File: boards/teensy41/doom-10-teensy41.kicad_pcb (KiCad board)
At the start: 4 copper layers, 172 x 68 mm, 73 parts, among them J1 SJ1-3525N, J2 S2B-PH-K-S(LF)(SN), J5 S2B-PH-K-S(LF)(SN), SW12 JS102011SAQN, U1 TEENSY41, U2 PCM5102APWR, U3 PAM8403DR, U4 BQ24074RGTR, U5 MAX17048G+T10, U6 TPS61023DRLR

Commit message: PCBKit's mark and pcbkit.io on every board; the RP2350 handheld ready to order
The handheld runs from two 18650 cells in parallel behind a DW01A protector and a reverse-cell
P-MOSFET, charged at up to 500 mA from the Pico's USB-C by a BQ24075 (power path into VSYS, timers
off for 6 Ah), with an on/off switch on 3V3_EN, M3 holes, ground pours and the console on pads.
Every assembled part has a JLCPCB code in stock (Basic where there is one); the module sockets are
in the BOM, the modules listed in the order's README. Check complete, the ready review clean.
Every board: routed and checked complete with the new mark.
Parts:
- added logo: , Logo_PCBKit_pcbkit.io, F.Cu at (294.8, 197.0)
- SW1, SW10, SW2, SW3, SW4, SW5, SW6, SW7, SW8, SW9: value (none) -> PTS645SM43SMTR92 LFS

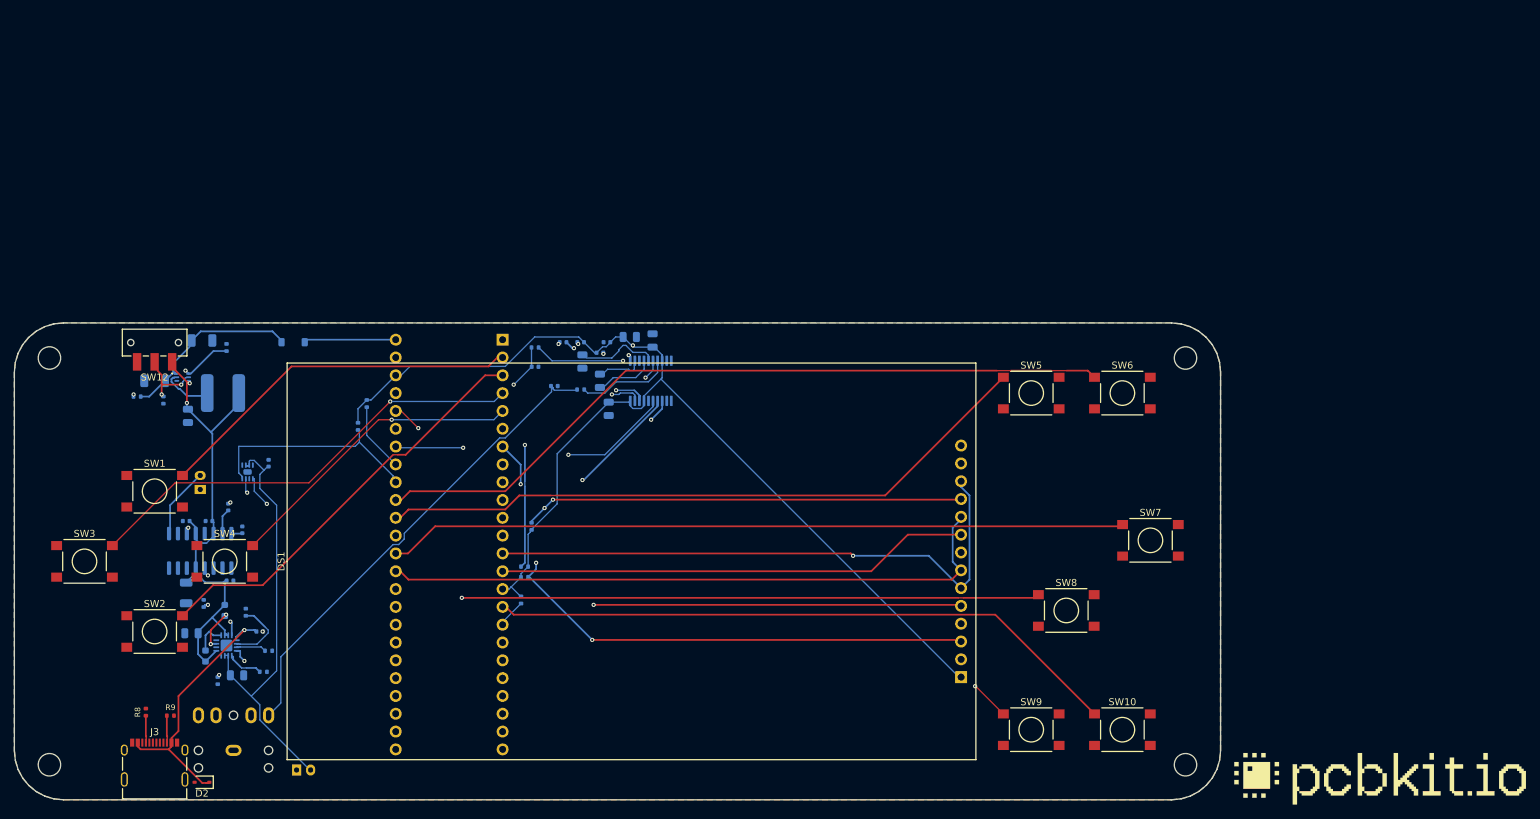
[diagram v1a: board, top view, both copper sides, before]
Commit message: teensy41: two 18650 cells with protection and a power-path charger; every part orderable
The LiPo on a JST plug and its BQ24074 become two 18650 in parallel (Keystone 1042 holders on the
back, right of the Teensy so its microSD card comes out) behind a reverse-cell P-FET and
DW01A + FS8205A protection, charged by a BQ24075 with power path from the board's USB-C (now with
a 1 A PTC and a TVS); the TPS61023 boost to the Teensy's VIN, the amplifier and the MAX17048 fuel
gauge run from the power path and the cells; the on/off switch drives the boost's EN. Board
172 x 112 mm, 4 layers, M3 holes, test pads, the speaker plug and the jack on the edges; the DAC's
and the amplifier's supplies decoupled at their pins; every assembled part pinned to an LCSC code;
the README says how to charge and flash.
check: complete, 0 errors, 0 warnings; ready lens: nothing to fix; fab export without --force.
Measured with doom-prod-a (52798750, 2bad2eb4: the fuse's ends no longer turned by the router,
stitching vias not flagged).

Claude-Session: https://claude.ai/code/session_01ATmMmxyrWxFwR3nTdXUrcx
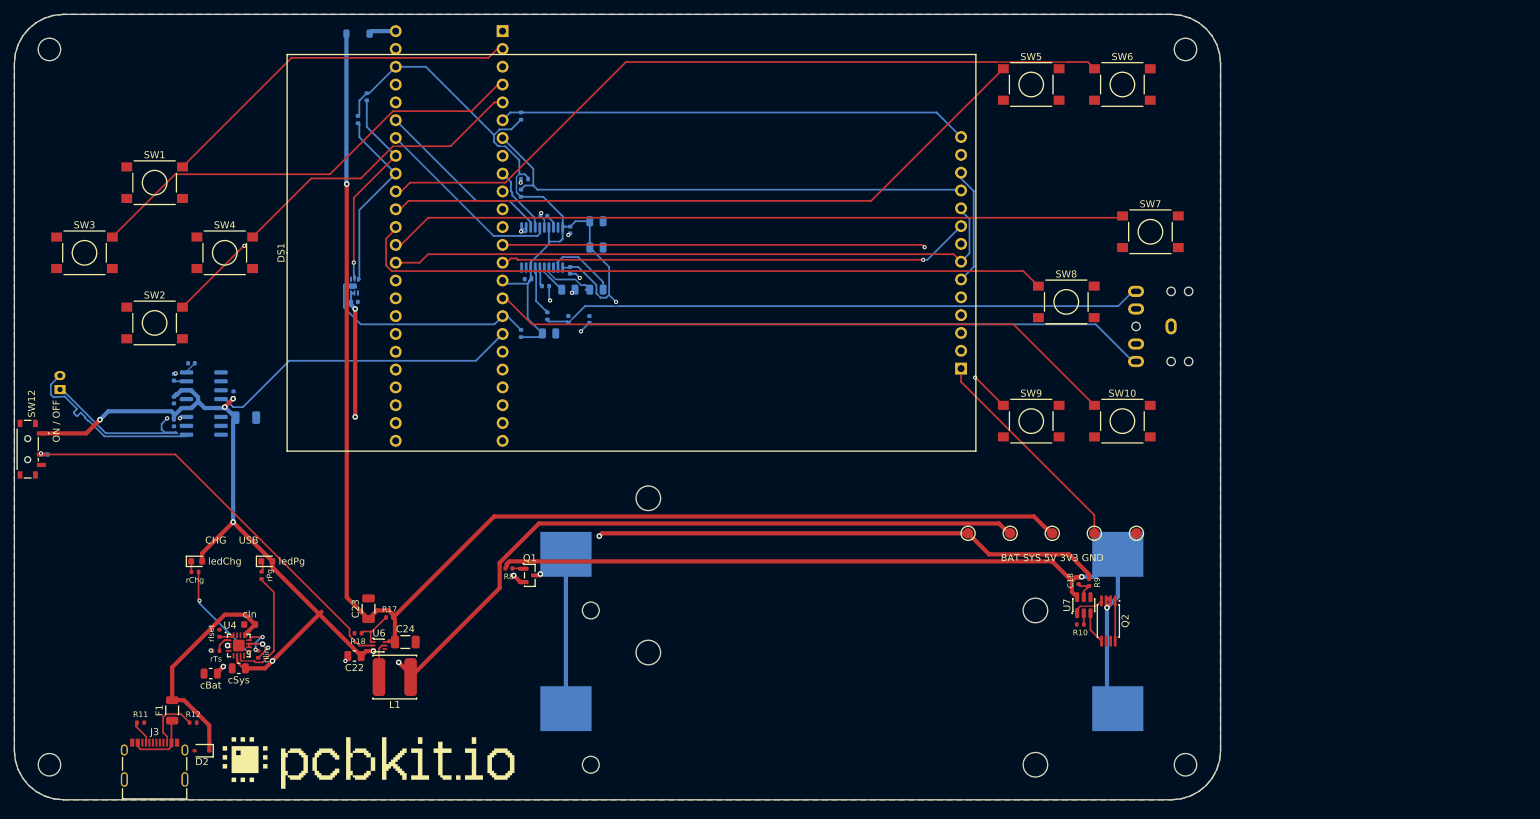
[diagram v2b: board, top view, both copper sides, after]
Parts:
- removed C19, C20: 4.7uF, C_0805_2012Metric
- removed D3: red, LED_0603_1608Metric
- removed D4: green, LED_0603_1608Metric
- removed J2: S2B-PH-K-S(LF)(SN), JST_PH_S2B-PH-K_1x02_P2.00mm_Horizontal
- removed R13: 46.4kohm, R_0402_1005Metric
- removed R14: 10kohm, R_0402_1005Metric
- added BT1: 1042, BatteryHolder_Keystone_1042_1x18650, B.Cu at (218.0, 187.0)
- added BT2: 1042, BatteryHolder_Keystone_1042_1x18650, B.Cu at (218.0, 165.0)
- added F1: PTC 1000mA, Fuse_1206_3216Metric, F.Cu at (122.5, 187.2)
- added Q1: AO3401A, SOT-23, F.Cu at (173.5, 168.0)
- added Q2: FS8205A, TSSOP-8_4.4x2.93mm_P0.65mm, F.Cu at (256.0, 174.5)
- added U7: DW01A, SOT-6_1.6x2.9mm_P0.95mm, F.Cu at (252.5, 172.2)
- added cBat: 4.7uF, C_0805_2012Metric, F.Cu at (128.0, 182.0)
- added cIn: 1uF, C_0603_1608Metric, F.Cu at (133.6, 175.0)
- added cSys: 4.7uF, C_0805_2012Metric, F.Cu at (132.0, 181.2)
- added ledChg: red, LED_0603_1608Metric, F.Cu at (126.0, 166.0)
- added ledPg: green, LED_0603_1608Metric, F.Cu at (136.0, 166.0)
- added rChg: 1.5kohm, R_0402_1005Metric, F.Cu at (125.8, 167.5)
- added rIlim: 1.18kohm, R_0402_1005Metric, F.Cu at (134.8, 179.2)
- added rIset: 1.13kohm, R_0402_1005Metric, F.Cu at (129.2, 176.2)
- added rPg: 1.5kohm, R_0402_1005Metric, F.Cu at (135.2, 168.0)
- added rTs: 10kohm, R_0402_1005Metric, F.Cu at (128.8, 178.8)
- added tpBat: , TestPoint_Round_D1.5mm, F.Cu at (236.0, 162.0)
- added tpGnd: , TestPoint_Round_D1.5mm, F.Cu at (260.0, 162.0)
- added tpSys: , TestPoint_Round_D1.5mm, F.Cu at (242.0, 162.0)
- added tpV3: , TestPoint_Round_D1.5mm, F.Cu at (254.0, 162.0)
- added tpV5: , TestPoint_Round_D1.5mm, F.Cu at (248.0, 162.0)
- C18: value 1uF -> 100nF; moved to F.Cu
- C22, C23, C24, L1, R17, R18, U6: moved to F.Cu
- D1: value schottky -> 1N5819HW-7-F
- R10: value 1.13kohm -> 1kohm; moved to F.Cu
- R11: value 1.18kohm -> 5.1kohm; moved to F.Cu
- R12: value 4.12kohm -> 5.1kohm; moved to F.Cu
- R8: value 5.1kohm -> 100kohm
- R9: value 5.1kohm -> 100ohm
- SW12: value JS102011SAQN -> MSK12C02; footprint SW_Slide_SPDT_CK_JS102011SAQN_Horizontal -> SW_Slide_SPDT_Shouhan_MSK12C02
- U4: value BQ24074RGTR -> BQ24075RGTR; moved to F.Cu
- moved J1 151.4 mm to (268.4, 132.5), turned to 270 degrees
- moved logo 144.3 mm to (150.5, 194.8)
- moved R9 132.4 mm to (253.2, 169.0), turned to 270 degrees
- moved R10 123.3 mm to (252.0, 175.0), turned to 180 degrees
- moved C18 117.0 mm to (251.8, 168.8), turned to 90 degrees
- moved R2 64.3 mm to (172.2, 102.5), turned to 270 degrees
- moved R3 56.8 mm to (172.8, 111.5), turned to 0 degrees
- moved R8 55.7 mm to (170.5, 167.0), turned to 180 degrees
- moved C24 51.6 mm to (155.8, 177.5)
- moved R17 47.8 mm to (153.5, 174.0), turned to 0 degrees
- moved R1 47.5 mm to (172.2, 113.5), turned to 270 degrees
- moved U6 47.4 mm to (152.0, 178.0)
- moved L1 47.3 mm to (154.2, 182.5), turned to 180 degrees
- moved C23 45.0 mm to (150.5, 172.8), turned to 90 degrees
- moved D1 45.0 mm to (149.0, 90.8)
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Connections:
- net Net-(C8-1) renamed DAC_VNEG
- net Net-(C9-1) renamed DAC_LDO
- C12 pad 1: VSYS -> SYS
- C13 pad 1: VSYS -> SYS
- C14 pad 1: VSYS -> SYS
- C15 pad 1: VSYS -> SYS
- C17 pad 1: Net-(C17-1) -> LINE_L
- C17 pad 2: LINE_L -> Net-(C17-1)
- C18 pad 1: VBUS -> Net-(C18-1)
- C18 pad 2: GND -> CELL_N
- C21 pad 1: VBAT -> BAT
- C22 pad 1: VSYS -> SYS
- J3 pad A4: VBUS -> usb/raw
- J3 pad B4: VBUS -> usb/raw
- L1 pad 1: VSYS -> SYS
- R1 pad 1: T_CS -> V3
- R1 pad 2: V3 -> T_CS
- R11 pad 1: Net-(R11-1) -> usb/cc1
- R12 pad 1: Net-(R12-1) -> usb/cc2
- R4 pad 1: FUEL_ALRT -> V3
- R4 pad 2: V3 -> FUEL_ALRT
- R6 pad 1: LINE_L -> Net-(R6-1)
- R6 pad 2: Net-(R6-1) -> LINE_L
- R7 pad 1: Net-(R7-1) -> LINE_R
- R7 pad 2: LINE_R -> Net-(R7-1)
- R8 pad 1: usb/cc1 -> reversed/gate
- R8 pad 2: GND -> CELL_N
- R9 pad 1: usb/cc2 -> BAT
- R9 pad 2: GND -> Net-(C18-1)
- SW12 pad 1: VSYS -> SYS
- U3 pad 13: VSYS -> SYS
- U3 pad 4: VSYS -> SYS
- U3 pad 6: VSYS -> SYS
- U4 pad 1: Net-(R14-1) -> TS
- U4 pad 10: VSYS -> SYS
- U4 pad 11: VSYS -> SYS
- U4 pad 12: Net-(R11-1) -> ILIM
- U4 pad 14: Net-(R13-1) -> GND
- U4 pad 15: Net-(R12-1) -> GND
- U4 pad 16: Net-(R10-1) -> ISET
- U4 pad 2: VBAT -> BAT
- U4 pad 3: VBAT -> BAT
- U4 pad 5: VSYS -> GND
- U4 pad 6: GND -> SYS
- U4 pad 7: Net-(D4-1) -> PG_N
- U4 pad 9: Net-(D3-1) -> CHG_N
- U5 pad 2: VBAT -> BAT
- U5 pad 3: VBAT -> BAT
- U6 pad 3: VSYS -> SYS
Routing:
- net SYS: track 0.00 -> 215.4 mm, vias 0 -> 8
- net BAT: track 0.00 -> 182.0 mm, vias 0 -> 6
- net V5: track 25.7 -> 194.9 mm, vias 0 -> 1
- net CELL_N: track 0.00 -> 117.5 mm, vias 0 -> 2
- net VSYS: track 72.1 -> 0.00 mm, vias 2 -> 0
- net LINE_L: track 86.0 -> 148.6 mm, vias 2 -> 3
- net VBAT: track 61.2 -> 0.00 mm
- net BOOST_EN: track 7.94 -> 59.2 mm, vias 2 -> 1
- net V3: track 165.7 -> 201.0 mm, vias 2 -> 1
- net BAT_IN: track 0.00 -> 22.0 mm, vias 0 -> 1
- net SPK_N: track 5.21 -> 25.5 mm, vias 1 -> 2
- net SPK_P: track 8.57 -> 26.8 mm
- net LINE_R: track 68.8 -> 86.7 mm
- net I2S_DIN: track 27.4 -> 9.61 mm, vias 1 -> 0
- net FUEL_ALRT: track 49.4 -> 31.8 mm, vias 1 -> 0
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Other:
- board size 172 x 68 mm -> 172 x 112 mm
- board text added: "+"
- board text added: "-"
- board text added: "2 x 18650 Li-ion 3.7 V"
- board text added: "BAT SYS 5V 3V3 GND"
- board text added: "CHG USB"
- board text added: "ON / OFF"
